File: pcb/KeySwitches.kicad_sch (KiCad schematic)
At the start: 2 parts

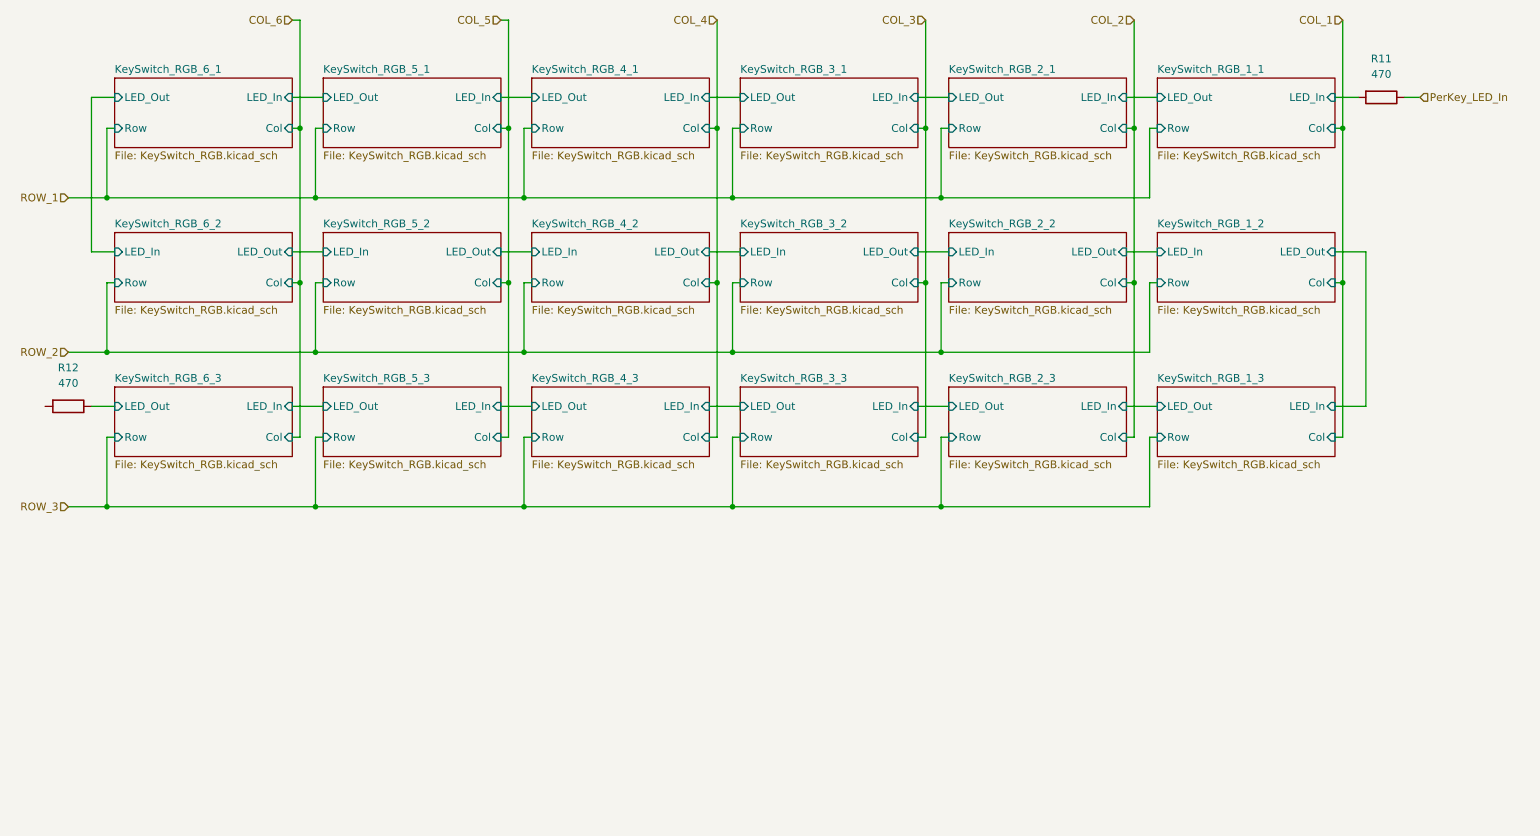
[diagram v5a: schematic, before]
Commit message: Adding reversible MX Sockets and SK6812MiniE footprints, finishing the replacement of Ethernet with a TRRS connector and selectable 0Ohm resistors to swap Rx/Tx for the interconnect.
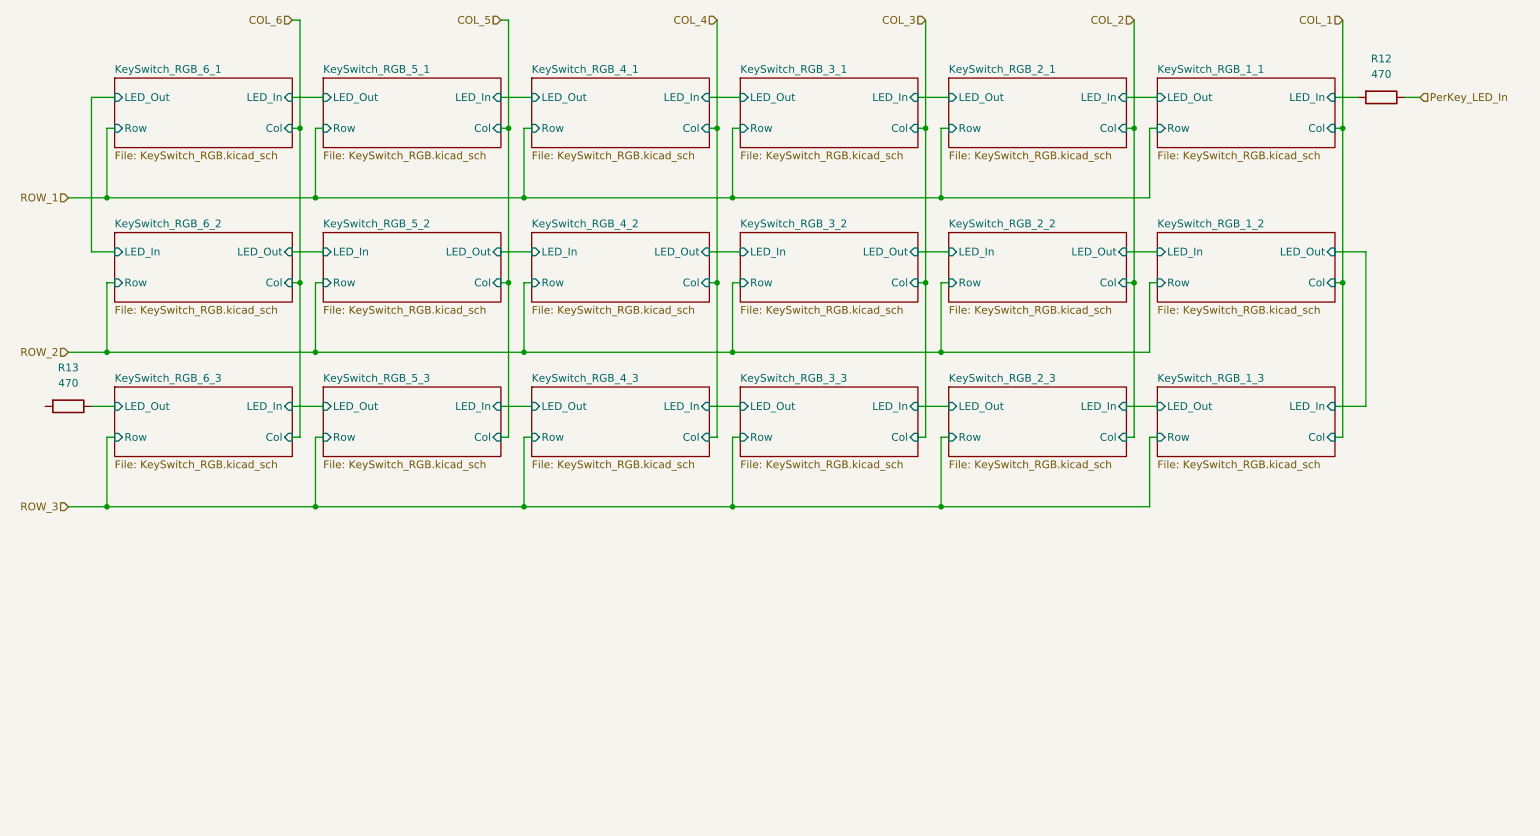
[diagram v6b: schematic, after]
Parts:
- renumbered R11 to R12, R12 to R13
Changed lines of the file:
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@@
 		(dnp no)
 		(fields_autoplaced yes)
-		(property "Reference" "R11"
+		(property "Reference" "R12"
 			(at 246.38 30.48 90)
 			(effects
@@
 			(project "cheapino"
 				(path "/9203b006-47ac-4f34-8cc4-2b709e3df56f/ef93f48f-e975-41f5-b90d-770a980a84dd"
-					(reference "R11")
+					(reference "R12")
 					(unit 1)
 				)
@@
 		(dnp no)
 		(fields_autoplaced yes)
-		(property "Reference" "R12"
+		(property "Reference" "R13"
 			(at 30.48 81.28 90)
 			(effects
@@
 			(project "cheapino"
 				(path "/9203b006-47ac-4f34-8cc4-2b709e3df56f/ef93f48f-e975-41f5-b90d-770a980a84dd"
-					(reference "R12")
+					(reference "R13")
 					(unit 1)
 				)

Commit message: Renumbering all reference designations and adding an initial layout for each keyswtich sub-pcb.
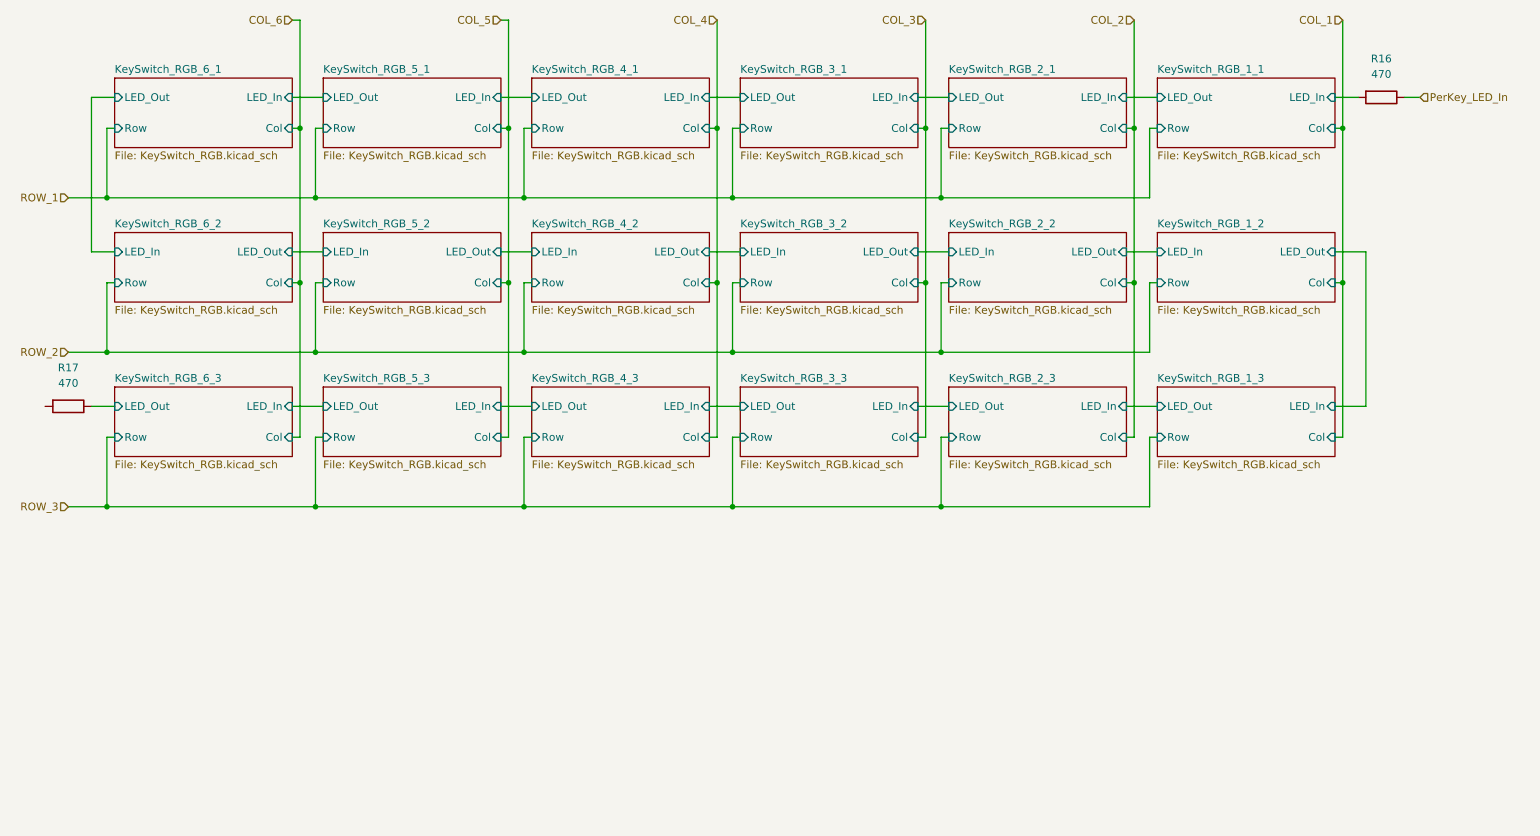
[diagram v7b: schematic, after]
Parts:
- renumbered R12 to R16, R13 to R17
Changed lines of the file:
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@@
 		(dnp no)
 		(fields_autoplaced yes)
-		(property "Reference" "R12"
+		(property "Reference" "R16"
 			(at 246.38 30.48 90)
 			(effects
@@
 			(project "cheapino"
 				(path "/9203b006-47ac-4f34-8cc4-2b709e3df56f/ef93f48f-e975-41f5-b90d-770a980a84dd"
-					(reference "R12")
+					(reference "R16")
 					(unit 1)
 				)
@@
 		(dnp no)
 		(fields_autoplaced yes)
-		(property "Reference" "R13"
+		(property "Reference" "R17"
 			(at 30.48 81.28 90)
 			(effects
@@
 			(project "cheapino"
 				(path "/9203b006-47ac-4f34-8cc4-2b709e3df56f/ef93f48f-e975-41f5-b90d-770a980a84dd"
-					(reference "R13")
+					(reference "R17")
 					(unit 1)
 				)
@@
 			(project "cheapino"
 				(path "/9203b006-47ac-4f34-8cc4-2b709e3df56f/ef93f48f-e975-41f5-b90d-770a980a84dd"
-					(page "18")
+					(page "23")
 				)
 			)
@@
 			(project "cheapino"
 				(path "/9203b006-47ac-4f34-8cc4-2b709e3df56f/ef93f48f-e975-41f5-b90d-770a980a84dd"
-					(page "17")
+					(page "12")
 				)
 			)
@@
 			(project "cheapino"
 				(path "/9203b006-47ac-4f34-8cc4-2b709e3df56f/ef93f48f-e975-41f5-b90d-770a980a84dd"
-					(page "12")
+					(page "17")
 				)
 			)
@@
 			(project "cheapino"
 				(path "/9203b006-47ac-4f34-8cc4-2b709e3df56f/ef93f48f-e975-41f5-b90d-770a980a84dd"
-					(page "19")
+					(page "22")
 				)
 			)
@@
 			(project "cheapino"
 				(path "/9203b006-47ac-4f34-8cc4-2b709e3df56f/ef93f48f-e975-41f5-b90d-770a980a84dd"
-					(page "22")
+					(page "19")
 				)
 			)
@@
 			(project "cheapino"
 				(path "/9203b006-47ac-4f34-8cc4-2b709e3df56f/ef93f48f-e975-41f5-b90d-770a980a84dd"
-					(page "13")
+					(page "16")
 				)
 			)
@@
 			(project "cheapino"
 				(path "/9203b006-47ac-4f34-8cc4-2b709e3df56f/ef93f48f-e975-41f5-b90d-770a980a84dd"
-					(page "7")
+					(page "6")
 				)
 			)
@@
 			(project "cheapino"
 				(path "/9203b006-47ac-4f34-8cc4-2b709e3df56f/ef93f48f-e975-41f5-b90d-770a980a84dd"
-					(page "6")
+					(page "7")
 				)
 			)
@@
 			(project "cheapino"
 				(path "/9203b006-47ac-4f34-8cc4-2b709e3df56f/ef93f48f-e975-41f5-b90d-770a980a84dd"
-					(page "16")
+					(page "13")
 				)
 			)
@@
 			(project "cheapino"
 				(path "/9203b006-47ac-4f34-8cc4-2b709e3df56f/ef93f48f-e975-41f5-b90d-770a980a84dd"
-					(page "23")
-				)
-			)
+					(page "18")
+				)
+			)
